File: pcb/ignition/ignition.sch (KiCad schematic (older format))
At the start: 23 parts

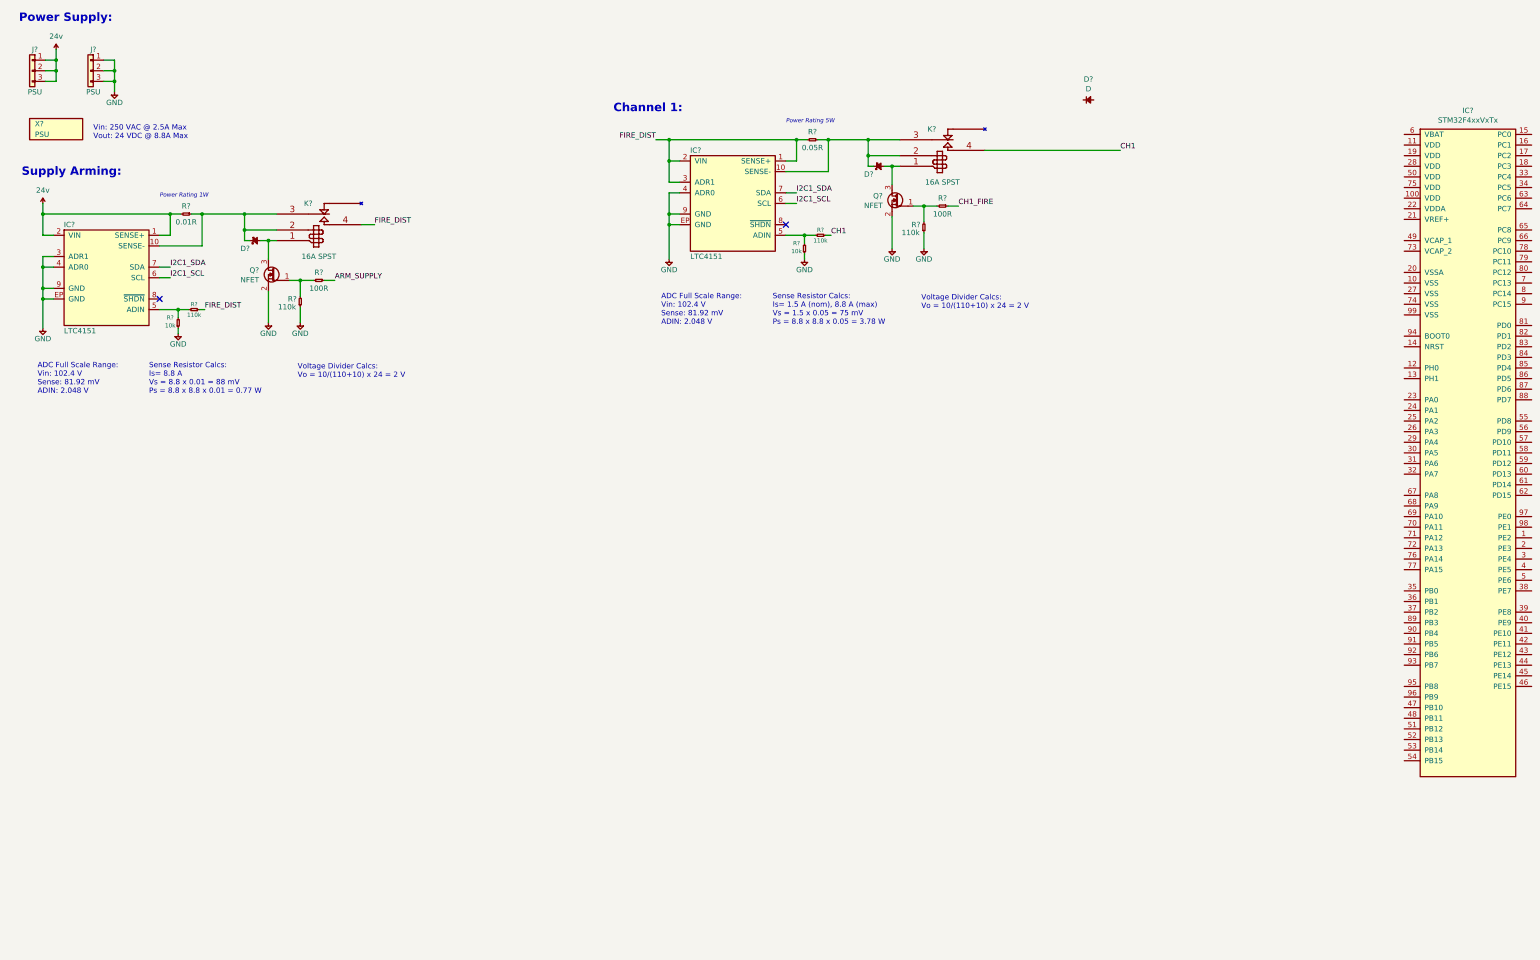
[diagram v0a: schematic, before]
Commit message: added valve channels
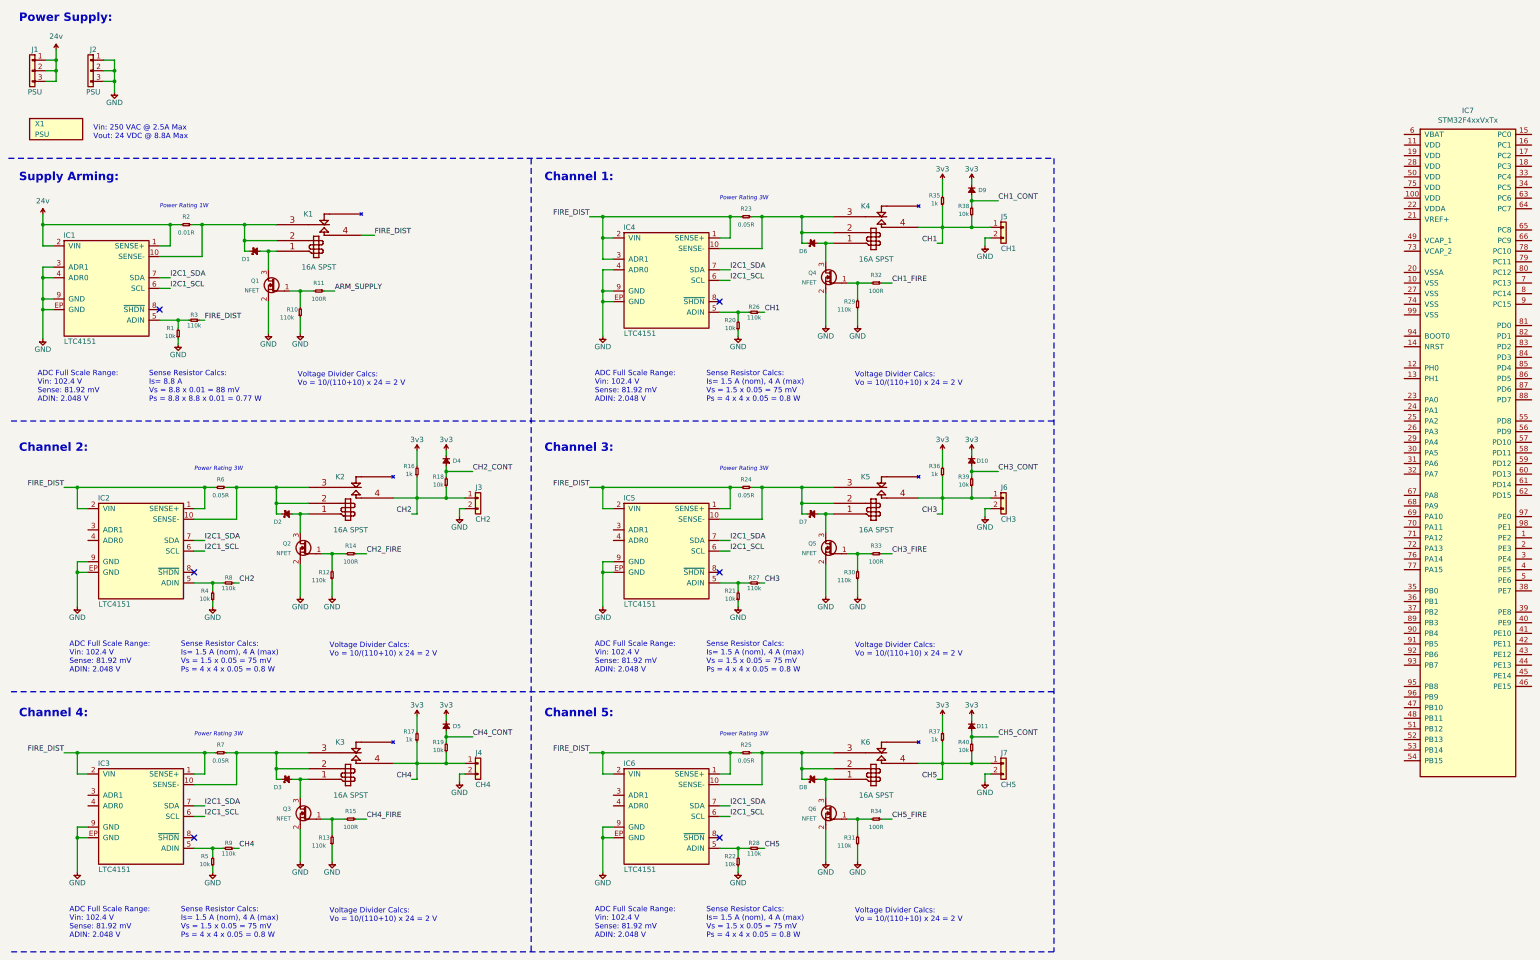
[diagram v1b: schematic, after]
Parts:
- removed R?: 100R, symbol agg-kicad:R
- removed R? (x2): 110k, symbol agg-kicad:R
- removed R?: 10k, symbol agg-kicad:R
- added D10, D11, D4, D5: D, ignition:SOD-123F, symbol agg-kicad:D
- added D2, D3, D7, D8: SCHOTTKY, ignition:SOD-123FL, symbol agg-kicad:SCHOTTKY
- added IC2, IC3, IC5, IC6: LTC4151, agg:DFN-10-EP-LT, symbol agg-kicad:LTC4151
- added J3: CH2, agg:S02B-PASK-2, symbol agg-kicad:CONN_01x02
- added J4: CH4, agg:S02B-PASK-2, symbol agg-kicad:CONN_01x02
- added J5: CH1, agg:S02B-PASK-2, symbol agg-kicad:CONN_01x02
- added J6: CH3, agg:S02B-PASK-2, symbol agg-kicad:CONN_01x02
- added J7: CH5, agg:S02B-PASK-2, symbol agg-kicad:CONN_01x02
- added K2, K3, K5, K6: 16A SPST, symbol relay_spst:RELAY_SPST
- added Q2, Q3, Q5, Q6: NFET, agg:SOT-23, symbol agg-kicad:NFET
- added R1, R18, R19, R21, R22, R38, R39, R4, R40, R5: 10k, agg:0603, symbol agg-kicad:R
- added R10, R12, R13, R27, R28, R3, R30, R31, R8, R9: 110k, agg:0603, symbol agg-kicad:R
- added R11, R14, R15, R33, R34: 100R, agg:0603, symbol agg-kicad:R
- added R16, R17, R35, R36, R37: 1k, agg:0603, symbol agg-kicad:R
- added R24, R25, R6, R7: 0.05R, agg:2512, symbol agg-kicad:R
- D1, D6: renamed from D?; footprint (none) -> ignition:SOD-123FL; Farnell (none) -> 2452032
- D9: renamed from D?; footprint (none) -> ignition:SOD-123F; Farnell (none) -> 1510671
- Q1, Q4: renamed from Q?; footprint (none) -> agg:SOT-23
- R2: renamed from R?; footprint (none) -> agg:2512
- R20: renamed from R?; footprint (none) -> agg:0603; Farnell (none) -> 2332016
- R23: renamed from R?; footprint (none) -> agg:2512; Farnell 1107481 -> 1435950
- R26, R29: renamed from R?; footprint (none) -> agg:0603; Farnell (none) -> 2138501
- R32: renamed from R?; footprint (none) -> agg:0603; Farnell (none) -> 2616742
- gave numbers to parts that had none: 8
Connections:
- net ARM_SUPPLY: now also R11.1
- net CH1: now also J5.1, R35.1, R38.1
- net FIRE_DIST: now also IC2.1 (SENSE+), IC2.2 (VIN), IC3.1 (SENSE+), IC3.2 (VIN), IC5.1 (SENSE+), IC5.2 (VIN), IC6.1 (SENSE+), IC6.2 (VIN), R24.2, R25.2, R3.1, R6.2, R7.2
- net GND: now also IC2.9 (GND), IC2.EP (GND), IC3.9 (GND), IC3.EP (GND), IC5.9 (GND), IC5.EP (GND), IC6.9 (GND), IC6.EP (GND), J3.2, J4.2, J5.2, J6.2, J7.2, Q2.2 (S), Q3.2 (S), Q5.2 (S), Q6.2 (S), R1.1, R10.1, R12.1, R13.1, R21.1, R22.1, R30.1, R31.1, R4.1, R5.1
- net I2C1_SCL: now also IC2.6 (SCL), IC3.6 (SCL), IC5.6 (SCL), IC6.6 (SCL)
- net I2C1_SDA: now also IC2.7 (SDA), IC3.7 (SDA), IC5.7 (SDA), IC6.7 (SDA)
- net at IC1.5 (ADIN): now also R1.2, R3.2
- net 3v3: now reaches D9.1
- net 3v3: now also D10.1, D11.1, D4.1, D5.1, R16.2, R17.2, R35.2, R36.2, R37.2
- net CH1_CONT: now reaches D9.2
- net CH1_CONT: now also R38.2
- net at Q1.1 (G): now also R10.2, R11.2
- new net: Q2.1 (G), R12.2, R14.2
- new net: D2.2, K2.1, Q2.3 (D)
- new net: D2.1, IC2.10 (SENSE-), K2.2, K2.3, R6.1
- new net: IC2.5 (ADIN), R4.2, R8.2
- new net: Q5.1 (G), R30.2, R33.2
- new net: D7.2, K5.1, Q5.3 (D)
- new net: D7.1, IC5.10 (SENSE-), K5.2, K5.3, R24.1
- new net: IC5.5 (ADIN), R21.2, R27.2
- new net: Q3.1 (G), R13.2, R15.2
- new net: D3.2, K3.1, Q3.3 (D)
- new net: D3.1, IC3.10 (SENSE-), K3.2, K3.3, R7.1
- new net: IC3.5 (ADIN), R5.2, R9.2
- new net: Q6.1 (G), R31.2, R34.2
- new net: D8.2, K6.1, Q6.3 (D)
- new net: D8.1, IC6.10 (SENSE-), K6.2, K6.3, R25.1
- new net: IC6.5 (ADIN), R22.2, R28.2
- new net CH2: J3.1, K2.4, R16.1, R18.1, R8.1
- new net CH2_CONT: D4.2, R18.2
- new net CH2_FIRE: R14.1
- new net CH3: J6.1, K5.4, R27.1, R36.1, R39.1
- new net CH3_CONT: D10.2, R39.2
- new net CH3_FIRE: R33.1
- new net CH4: J4.1, K3.4, R17.1, R19.1, R9.1
- new net CH4_CONT: D5.2, R19.2
- new net CH4_FIRE: R15.1
- new net CH5: J7.1, K6.4, R28.1, R37.1, R40.1
- new net CH5_CONT: D11.2, R40.2
- new net CH5_FIRE: R34.1
- no-connect marks 2 -> 6
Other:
- note added: "Channel 2:"
- note added: "Channel 3:"
- note added: "Channel 4:"
- note added: "Channel 5:"
- note added: "Power Rating 3W"
- note added: "Sense Resistor Calcs:\nIs= 1.5 A (nom), 4 A (max) \nVs = 1.5 x 0.05 = 75 mV\nPs = 4 x 4 x 0.05 = 0.8 W"
- note removed: "Power Rating 5W"
- note removed: "Sense Resistor Calcs:\nIs= 1.5 A (nom), 8.8 A (max) \nVs = 1.5 x 0.05 = 75 mV\nPs = 8.8 x 8.8 x 0.05 = 3.78 W"
- moved on the sheet: D1, D6, D9, IC1, IC4, K1, K4, Q1, Q4, R2, R20, R23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

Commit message: made progress
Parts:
- added J?: LED1, symbol agg-kicad:CONN_01x02
- added J?: LED2, symbol agg-kicad:CONN_01x02
- added J?: LED3, symbol agg-kicad:CONN_01x02
- added J?: LED4, symbol agg-kicad:CONN_01x02
- added J?: LED5, symbol agg-kicad:CONN_01x02
- added J?: ARM, symbol agg-kicad:CONN_01x02
- added J?: PSU, symbol agg-kicad:CONN_01x02
- added R? (x6): 56R, agg:0603, symbol agg-kicad:R
- added R?: 110k, agg:0603, symbol agg-kicad:R
- added R?: 10k, agg:0603, symbol agg-kicad:R
- added X? (x5): GRN LED, symbol agg-kicad:PART
- added X? (x5): LED Bezel, symbol agg-kicad:PART
- added X?: 5V PSU, symbol agg-kicad:PART
- added X?: Key Switch, symbol agg-kicad:PART
- added X?: AC Input, symbol agg-kicad:PART
- X1: value PSU -> 24V PSU
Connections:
- net 3v3: now also R?.2, R?.2, R?.2, R?.2, R?.2
- net FIRE_DIST: now also IC2.3 (ADR1), IC2.4 (ADR0), IC3.4 (ADR0), IC5.3 (ADR1); no longer IC4.3 (ADR1)
- net GND: now also IC3.3 (ADR1), IC4.3 (ADR1), IC5.4 (ADR0), IC6.4 (ADR0), J?.2, R?.2
- net I2C1_SCL: no longer IC2.6 (SCL), IC3.6 (SCL), IC4.6 (SCL), IC5.6 (SCL), IC6.6 (SCL)
- net I2C1_SDA: no longer IC2.7 (SDA), IC3.7 (SDA), IC4.7 (SDA), IC5.7 (SDA), IC6.7 (SDA)
- net VCC: now also R?.2
- net LED1: now reaches D6.2, K4.1, Q4.3 (D)
- net LED1: now also J?.2
- net LED2: now reaches D2.2, K2.1, Q2.3 (D)
- net LED2: now also J?.2
- net LED3: now reaches D7.2, K5.1, Q5.3 (D)
- net LED3: now also J?.2
- net LED4: now reaches D3.2, K3.1, Q3.3 (D)
- net LED4: now also J?.2
- net LED5: now reaches D8.2, K6.1, Q6.3 (D)
- net LED5: now also J?.2
- new net: J?.1, R?.1 (x6)
- new net 5v: J?.1
- new net I2C2_SCL: IC2.6 (SCL), IC3.6 (SCL), IC4.6 (SCL), IC5.6 (SCL), IC6.6 (SCL)
- new net I2C2_SDA: IC2.7 (SDA), IC3.7 (SDA), IC4.7 (SDA), IC5.7 (SDA), IC6.7 (SDA)
- new net PSU_MON: R?.1, R?.1
- no-connect marks 6 -> 7
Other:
- note added: "2.2v 20mA"
- note added: "ADR: 0xCE\n"
- note added: "ADR: 0xD2"
- note added: "ADR: 0xD6\n"
- note added: "ADR: 0xD8\n"
- note added: "ADR: 0xDE"
- note added: "Panel Indicators:"
- note added: "The 5v PSU will be powered directly of the AC input \nso that the low voltage circuitry is always on. \nThe AC supply for the 24v PSU will go through a key \nswitch."
- note added: "Vin: 250 VAC @ 0.5A Max\nVout: 5 VDC @ 7A Max"
- note added: "add RGB arm LED"
- note added: "add caps"
- moved on the sheet: D1, IC1, J1, J2, K1, Q1, Q2, Q3, Q4, Q5, Q6, R1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

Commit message: finished schematic
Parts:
- removed IC7: STM32F4xxVxTx, agg:LQFP-100, symbol agg-kicad:STM32F4xxVxTx
- removed J1, J2: PSU, agg:S03B-PASK-2, symbol agg-kicad:CONN_01x03
- removed J3: CH2, agg:S02B-PASK-2, symbol agg-kicad:CONN_01x02
- removed J4: CH4, agg:S02B-PASK-2, symbol agg-kicad:CONN_01x02
- removed J5: CH1, agg:S02B-PASK-2, symbol agg-kicad:CONN_01x02
- removed J7: CH5, agg:S02B-PASK-2, symbol agg-kicad:CONN_01x02
- added C1, C2: 10u, agg:1206, symbol agg-kicad:C
- added C10, C11, C13, C14, C15, C16, C19, C20, C9: 100n, agg:0402, symbol agg-kicad:C
- added C12: 1µ, agg:0402, symbol agg-kicad:C
- added C17, C18: 2µ2, agg:0402, symbol agg-kicad:C
- added C3, C5: 1u, agg:0603-L, symbol agg-kicad:C
- added C4: 10n, agg:0603-L, symbol agg-kicad:C
- added C6, C7: 10p, agg:0402, symbol agg-kicad:C
- added C8: 4µ7, agg:0402, symbol agg-kicad:C
- added D10, D9: LED, agg:0603-LED, symbol agg-kicad:LED
- added IC7: ADP3335, agg:MSOP-8, symbol agg-kicad:ADP3335
- added IC8: STM32F437VIT6, agg:LQFP-100, symbol agg-kicad:STM32F4xxVxTx
- added J1, J3: PSU, ignition:172316-1104, symbol agg-kicad:CONN_01x04
- added J10: CH2, ignition:172316-1104, symbol agg-kicad:CONN_01x04
- added J11: CH4, ignition:172316-1104, symbol agg-kicad:CONN_01x04
- added J13: UART1, agg:S03B-PASK-2, symbol agg-kicad:CONN_01x03
- added J14: UART2, agg:S03B-PASK-2, symbol agg-kicad:CONN_01x03
- added J15: CH1, ignition:172316-1104, symbol agg-kicad:CONN_01x04
- added J16: CH3, ignition:172316-1104, symbol agg-kicad:CONN_01x04
- added J17: CH5, ignition:172316-1104, symbol agg-kicad:CONN_01x04
- added P1: SWD_TC, agg:TC2030-NL, symbol agg-kicad:SWD_TC
- added R37, R46: 100R, agg:0603, symbol agg-kicad:R
- added R41, R45, R47, R48: 1k, agg:0603, symbol agg-kicad:R
- added R55, R56, R57, R58, R59: 47k, agg:0603-L, symbol agg-kicad:R
- added R60: 100, agg:0402, symbol agg-kicad:R
- added TP1, TP2, TP3, TP4, TP5: TESTPAD, agg:TESTPAD, symbol agg-kicad:TESTPAD
- added U1: MICROSD, agg:MICROSD_MOLEX_503398-1892, symbol agg-kicad:MICROSD
- added X1, X16, X19, X24, X27, X30: Molex Wire, symbol agg-kicad:PART
- added X17, X20, X25, X28, X31: M12 Socket, symbol agg-kicad:PART
- added X18, X21, X26, X29, X32: M12 Plug, symbol agg-kicad:PART
- added X22: Bi-LED, symbol agg-kicad:PART
- added X23: LED Bezel, symbol agg-kicad:PART
- added X33, X34, X35, X36: Hole, agg:M3_MOUNT, symbol agg-kicad:PART
- added Y1: 26M, agg:XTAL-20x16, symbol agg-kicad:SMD_XTAL
- J12, J2, J4, J7, J8, J9: renamed from J?; footprint (none) -> agg:S02B-PASK-2; Farnell (none) -> 1830747
- J5: renamed from J?; value PSU -> 5v In; footprint (none) -> agg:S02B-PASK-2; Farnell (none) -> 1830747
- J6: value CH3 -> 5v Out; Farnell (none) -> 1830747
- K1: renamed from K2; footprint (none) -> ignition:RT33L024
- K2: renamed from K3; footprint (none) -> ignition:RT33L024
- K3: renamed from K1; footprint (none) -> ignition:RT33L024
- K4, K5, K6: footprint (none) -> ignition:RT33L024
- R27: renamed from R?; value 56R -> 100R; Farnell 2447400 -> 2616742
- X8: renamed from X?; Digikey 1145-1076-ND -> (none); Mouser (none) -> 653-A165K-T2ML-2
- X9: renamed from X?; Digikey 1145-1076-ND -> (none); Farnell (none) -> 2334072
- gave numbers to parts that had none: 18
- renumbered D2 to D1, D9 to D11, D10 to D12, D11 to D13, D3 to D2, D1 to D3, IC2 to IC1, IC3 to IC2, IC1 to IC3, Q2 to Q1, Q3 to Q2, Q1 to Q3, R9 to R10, R1 to R11, R2 to R13, R3 to R14, R12 to R15, R13 to R16, R14 to R18, R15 to R19, R10 to R20, R11 to R21, R16 to R22, R17 to R23, R18 to R25, R19 to R26, R20 to R28, R21 to R29, R22 to R30, R23 to R31, R24 to R32, R25 to R33, R26 to R34, R27 to R35, R28 to R36, R29 to R38, R30 to R39, R31 to R40, R32 to R42, R33 to R43, R34 to R44, R35 to R49, R4 to R5, R36 to R50, R37 to R51, R38 to R52, R39 to R53, R40 to R54, R5 to R6, R6 to R7, R7 to R8, R8 to R9, X1 to X12
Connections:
- net 3v3: now also C10.2, C11.2, C12.2, C13.2, C14.2, C15.2, C16.2, C19.1, C4.1, C5.1, C8.2, C9.2, IC7.1 (OUT), IC7.2 (OUT), IC7.3 (OUT), IC8.100 (VDD), IC8.11 (VDD), IC8.19 (VDD), IC8.21 (VREF+), IC8.22 (VDDA), IC8.28 (VDD), IC8.50 (VDD), IC8.6 (VBAT), IC8.75 (VDD), P1.1 (VDD), R37.1, R41.2, R45.2, R47.2, R48.2, R55.1, R56.1, R57.1, R58.1, R59.1, TP1.1 (TP), U1.4 (VDD)
- net 5v: now also J6.1, C2.1, C3.1, IC7.6 (SD), IC7.7 (IN), IC7.8 (IN)
- net ARM_SUPPLY: now also IC8.55 (PD8)
- net CH1: now also J15.1, J15.2
- net CH1_CONT: now also IC8.15 (PC0)
- net CH1_FIRE: now also IC8.56 (PD9)
- net CH2: now also J10.1, J10.2
- net CH2_CONT: now also IC8.16 (PC1)
- net CH2_FIRE: now also IC8.57 (PD10)
- net CH3: now also J16.1, J16.2; no longer J6.1
- net CH3_CONT: now also IC8.17 (PC2)
- net CH3_FIRE: now also IC8.58 (PD11)
- net CH4: now also J11.1, J11.2
- net CH4_CONT: now also IC8.18 (PC3)
- net CH4_FIRE: now also IC8.59 (PD12)
- net CH5: now also J17.1, J17.2
- net CH5_CONT: now also IC8.33 (PC4)
- net CH5_FIRE: now also IC8.60 (PD13)
- net GND: now also C1.2, C10.1, C11.1, C12.1, C13.1, C14.1, C15.1, C16.1, C17.2, C18.2, C19.2, C2.2, C20.1, C3.2, C5.2, C6.1, C7.1, C8.1, C9.1, D10.1, D9.1, IC7.4 (GND), IC8.10 (VSS), IC8.20 (VSSA), IC8.27 (VSS), IC8.74 (VSS), IC8.94 (BOOT0), IC8.99 (VSS), J10.3, J10.4, J11.3, J11.4, J13.3, J14.3, J15.3, J15.4, J16.3, J16.4, J17.3, J17.4, J3.1, J3.2, J3.3, J3.4, P1.5 (GND), U1.6 (VSS), U1.9 (SHIELD), Y1.2, Y1.4
- net I2C1_SCL: now also IC8.95 (PB8), R47.1, TP4.1 (TP)
- net I2C1_SDA: now also IC8.96 (PB9), R48.1, TP5.1 (TP)
- net I2C2_SCL: now also IC8.47 (PB10), R41.1, TP2.1 (TP)
- net I2C2_SDA: now also IC8.48 (PB11), R45.1, TP3.1 (TP)
- net PSU_MON: now also IC8.34 (PC5)
- net VCC: now also C1.1, J1.1, J1.2, J1.3, J1.4
- net ARM_RED: now reaches J12.2
- net ARM_RED: now also IC8.40 (PE9)
- net ARM_GRN: now reaches R27.2
- net ARM_GRN: now also IC8.39 (PE8)
- new net: C6.2, IC8.12 (PH0), Y1.1
- new net: IC8.13 (PH1), R60.2
- new net: C18.1, IC8.49 (VCAP_1)
- new net: C17.1, IC8.73 (VCAP_2)
- new net: C7.2, R60.1, Y1.3
- new net: C4.2, IC7.5 (NR)
- new net: D9.2, R37.2
- new net: D10.2, R46.2
- new net SDIO_CK: IC8.80 (PC12), U1.5 (CLK)
- new net SDIO_CMD: IC8.83 (PD2), R59.2, U1.3 (CMD)
- new net SDIO_D0: IC8.65 (PC8), R55.2, U1.7 (DAT0)
- new net SDIO_D1: IC8.66 (PC9), R56.2, U1.8 (DAT1)
- new net SDIO_D2: IC8.78 (PC10), R57.2, U1.1 (DAT2)
- new net SDIO_D3: IC8.79 (PC11), R58.2, U1.2 (DAT3)
- new net STATUS: IC8.43 (PE12), R46.1
- new net SWDCLK: IC8.76 (PA14), P1.4 (SWDCLK)
- new net SWDIO: IC8.72 (PA13), P1.2 (SWDIO)
- new net USART1_RX: IC8.69 (PA10), J13.2
- new net USART1_TX: IC8.68 (PA9), J13.1
- new net USART2_RX: IC8.26 (PA3), J14.2
- new net USART2_TX: IC8.25 (PA2), J14.1
- new net ~RST: C20.2, IC8.14 (NRST), P1.3 (~RST)
- no-connect marks 7 -> 59
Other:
- note added: "1.8v 20mA"
- note added: "ADC12 IN 10-15"
- note added: "Communication Ports:"
- note added: "External Power Supply:"
- note added: "High Speed I2C Pullups"
- note added: "Microcontroller:"
- note added: "SD Card:"
- note added: "Tag Connect:"
- note removed: "add RGB arm LED"
- note removed: "add caps"
- moved on the sheet: J12, J5, R27, X12, X13, X8, X9

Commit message: changed key switch
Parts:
- X8: Farnell (none) -> 51-235.025D2; Mouser 653-A165K-T2ML-2 -> (none)
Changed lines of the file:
@@
 F 2 "" H 3075 1025 50  0001 C CNN
 F 3 "https://www.mouser.co.uk/datasheet/2/307/a165k_ds_e_3_3_csm604-795238.pdf" H 3075 1025 50  0001 C CNN
-F 4 "653-A165K-T2ML-2" H 3075 1025 50  0001 C CNN "Mouser"
+F 4 "51-235.025D2" H 3075 1025 50  0001 C CNN "Farnell"
 	1    3075 1025
 	1    0    0    -1

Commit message: finalised schematic, started pcb component placement
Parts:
- IC1, IC2, IC3, IC4, IC5, IC6: footprint agg:DFN-10-EP-LT -> agg:MSOP-10; Digikey (none) -> LTC4151CMS-1#PBF-ND; Farnell 2295457 -> (none)
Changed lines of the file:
@@
 F 0 "IC3" H 1675 3700 50  0000 C CNN
 F 1 "LTC4151" H 1775 2700 50  0000 C CNN
-F 2 "agg:DFN-10-EP-LT" H 1625 2600 50  0001 L CNN
+F 2 "agg:MSOP-10" H 1625 2600 50  0001 L CNN
 F 3 "http://cds.linear.com/docs/en/datasheet/4151ff.pdf" H 1625 2500 50  0001 L CNN
-F 4 "2295457" H 1625 2400 50  0001 L CNN "Farnell"
+F 4 "LTC4151CMS-1#PBF-ND" H 1625 2400 50  0001 L CNN "Digikey"
 	1    2025 3200
 	1    0    0    -1
@@
 F 0 "IC4" H 6350 3625 50  0000 C CNN
 F 1 "LTC4151" H 6450 2625 50  0000 C CNN
-F 2 "agg:DFN-10-EP-LT" H 6300 2525 50  0001 L CNN
+F 2 "agg:MSOP-10" H 6300 2525 50  0001 L CNN
 F 3 "http://cds.linear.com/docs/en/datasheet/4151ff.pdf" H 6300 2425 50  0001 L CNN
-F 4 "2295457" H 6300 2325 50  0001 L CNN "Farnell"
+F 4 "LTC4151CMS-1#PBF-ND" H 6300 2325 50  0001 L CNN "Digikey"
 	1    6700 3125
 	1    0    0    -1
@@
 F 0 "IC1" H 1400 6175 50  0000 C CNN
 F 1 "LTC4151" H 1500 5175 50  0000 C CNN
-F 2 "agg:DFN-10-EP-LT" H 1350 5075 50  0001 L CNN
+F 2 "agg:MSOP-10" H 1350 5075 50  0001 L CNN
 F 3 "http://cds.linear.com/docs/en/datasheet/4151ff.pdf" H 1350 4975 50  0001 L CNN
-F 4 "2295457" H 1350 4875 50  0001 L CNN "Farnell"
+F 4 "LTC4151CMS-1#PBF-ND" H 1350 4875 50  0001 L CNN "Digikey"
 	1    1750 5675
 	1    0    0    -1
@@
 F 0 "IC5" H 6350 6175 50  0000 C CNN
 F 1 "LTC4151" H 6450 5175 50  0000 C CNN
-F 2 "agg:DFN-10-EP-LT" H 6300 5075 50  0001 L CNN
+F 2 "agg:MSOP-10" H 6300 5075 50  0001 L CNN
 F 3 "http://cds.linear.com/docs/en/datasheet/4151ff.pdf" H 6300 4975 50  0001 L CNN
-F 4 "2295457" H 6300 4875 50  0001 L CNN "Farnell"
+F 4 "LTC4151CMS-1#PBF-ND" H 6300 4875 50  0001 L CNN "Digikey"
 	1    6700 5675
 	1    0    0    -1
@@
 F 0 "IC2" H 1400 8675 50  0000 C CNN
 F 1 "LTC4151" H 1500 7675 50  0000 C CNN
-F 2 "agg:DFN-10-EP-LT" H 1350 7575 50  0001 L CNN
+F 2 "agg:MSOP-10" H 1350 7575 50  0001 L CNN
 F 3 "http://cds.linear.com/docs/en/datasheet/4151ff.pdf" H 1350 7475 50  0001 L CNN
-F 4 "2295457" H 1350 7375 50  0001 L CNN "Farnell"
+F 4 "LTC4151CMS-1#PBF-ND" H 1350 7375 50  0001 L CNN "Digikey"
 	1    1750 8175
 	1    0    0    -1
@@
 F 0 "IC6" H 6350 8675 50  0000 C CNN
 F 1 "LTC4151" H 6450 7675 50  0000 C CNN
-F 2 "agg:DFN-10-EP-LT" H 6300 7575 50  0001 L CNN
+F 2 "agg:MSOP-10" H 6300 7575 50  0001 L CNN
 F 3 "http://cds.linear.com/docs/en/datasheet/4151ff.pdf" H 6300 7475 50  0001 L CNN
-F 4 "2295457" H 6300 7375 50  0001 L CNN "Farnell"
+F 4 "LTC4151CMS-1#PBF-ND" H 6300 7375 50  0001 L CNN "Digikey"
 	1    6700 8175
 	1    0    0    -1
